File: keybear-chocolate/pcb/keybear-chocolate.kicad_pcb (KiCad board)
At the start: 2 copper layers, 136.9 x 98.2 mm, 108 parts, among them J2 BATT, J3 LED, J4 OLED, P1 USB_C_Plug, SW1 SW_PUSH, SW10 SW_PUSH, SW11 SW_PUSH, SW12 SW_PUSH, SW13 SW_PUSH, SW14 SW_PUSH, SW15 SW_PUSH, SW16 SW_PUSH, SW17 SW_PUSH, SW18 SW_PUSH, SW19 SW_PUSH, SW2 SW_PUSH, SW20 SW_PUSH, SW21 SW_PUSH, SW22 SW_PUSH, SW24 Rotary_Encoder_Switch, SW3 SW_PUSH, SW30 BATT_SW, SW4 SW_PUSH, SW5 SW_PUSH, SW6 SW_PUSH, SW7 SW_PUSH, SW8 SW_PUSH, SW9 SW_PUSH, U1 ProMicro, U2 MCP23017_ML, U3 ATECC608A-SSHDA

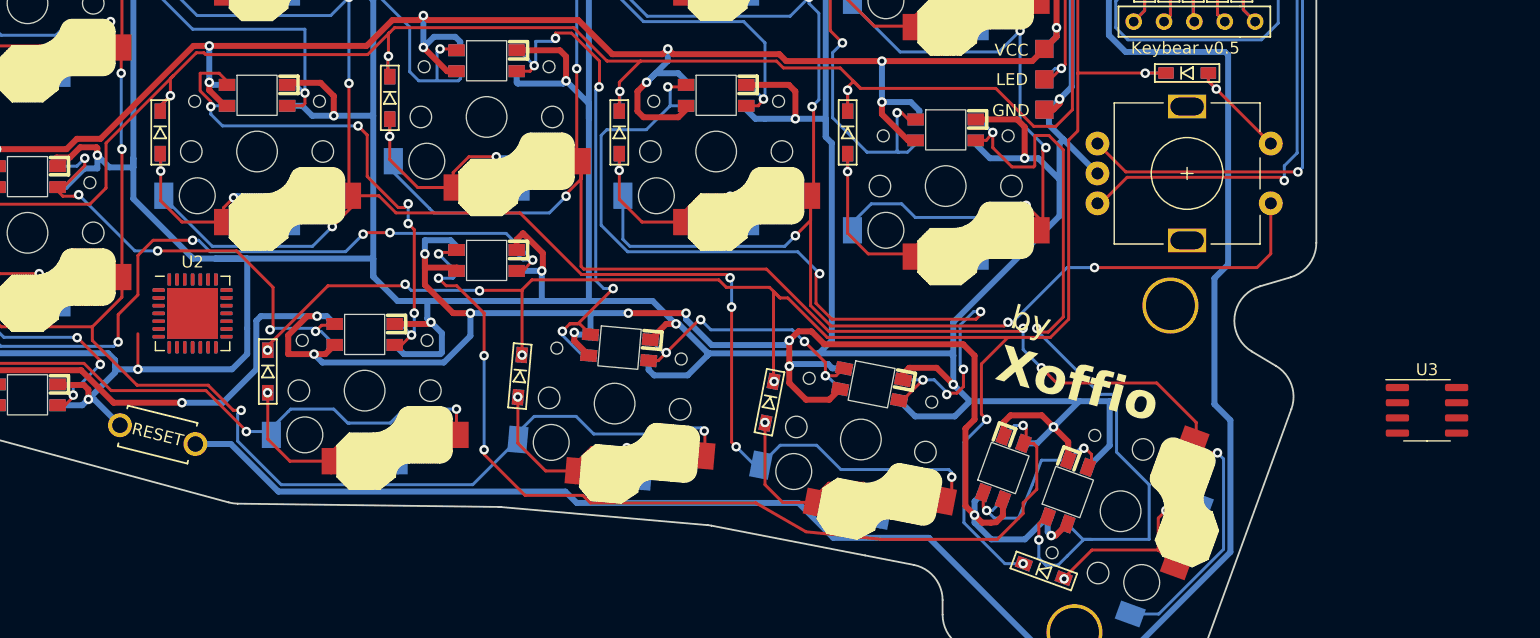
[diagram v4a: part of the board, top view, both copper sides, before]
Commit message: adding PCF8523 (Real Time Clock)
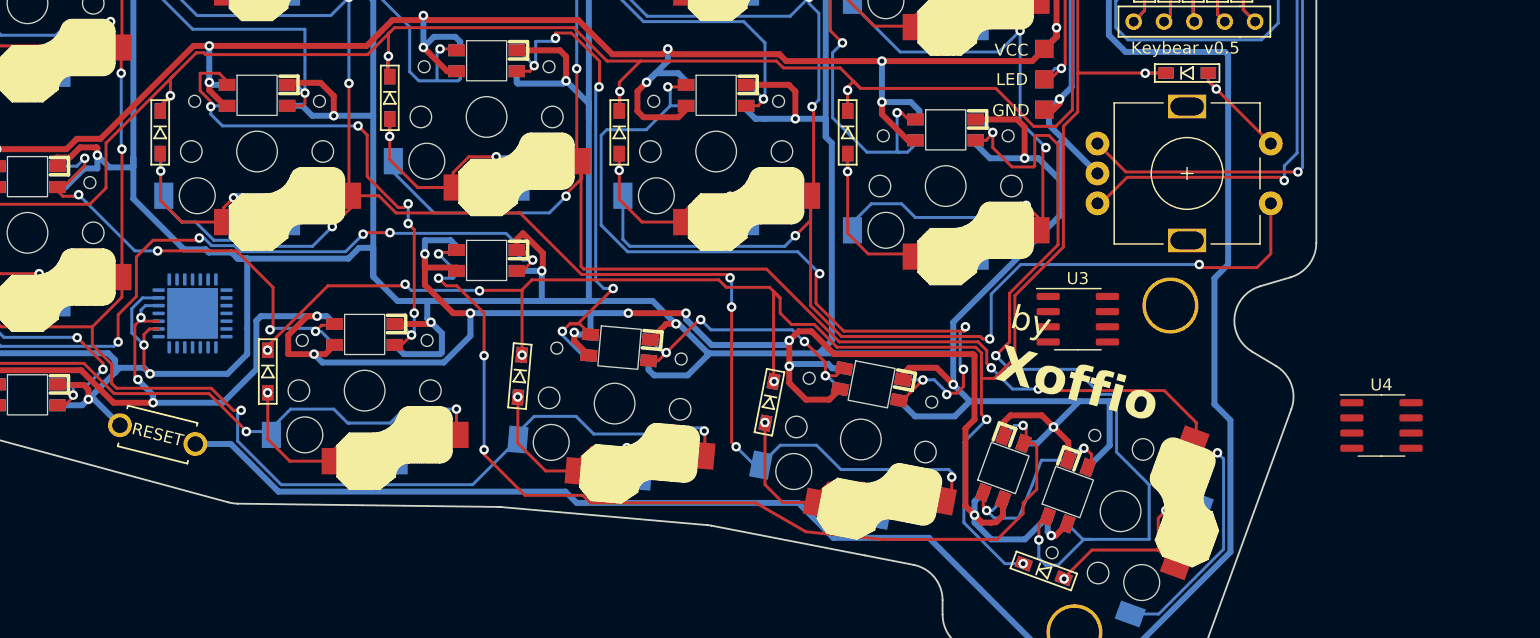
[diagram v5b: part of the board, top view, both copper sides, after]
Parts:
- removed the U2 at (183.0, 156.7)
- added U4: PCF8523T, Package_SO:SOIC-8_3.9x4.9mm_P1.27mm, F.Cu at (282.4, 166.1)
- moved U3 30.2 mm to (257.0, 157.2)
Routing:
- net VCC: track 894.5 -> 906.4 mm, vias 62 -> 64
- net GND: track 914.6 -> 922.4 mm, vias 34 -> 35
- net Net-(L18-DIN): track 71.0 -> 75.7 mm
- net SW24A: track 189.2 -> 192.5 mm
- net Net-(L17-DOUT): track 73.3 -> 70.2 mm
- net col1: track 258.7 -> 259.9 mm
- net row3: track 168.7 -> 169.6 mm
- net col3: track 234.7 -> 234.1 mm
- net Net-(L27-DIN): track 87.3 -> 87.8 mm

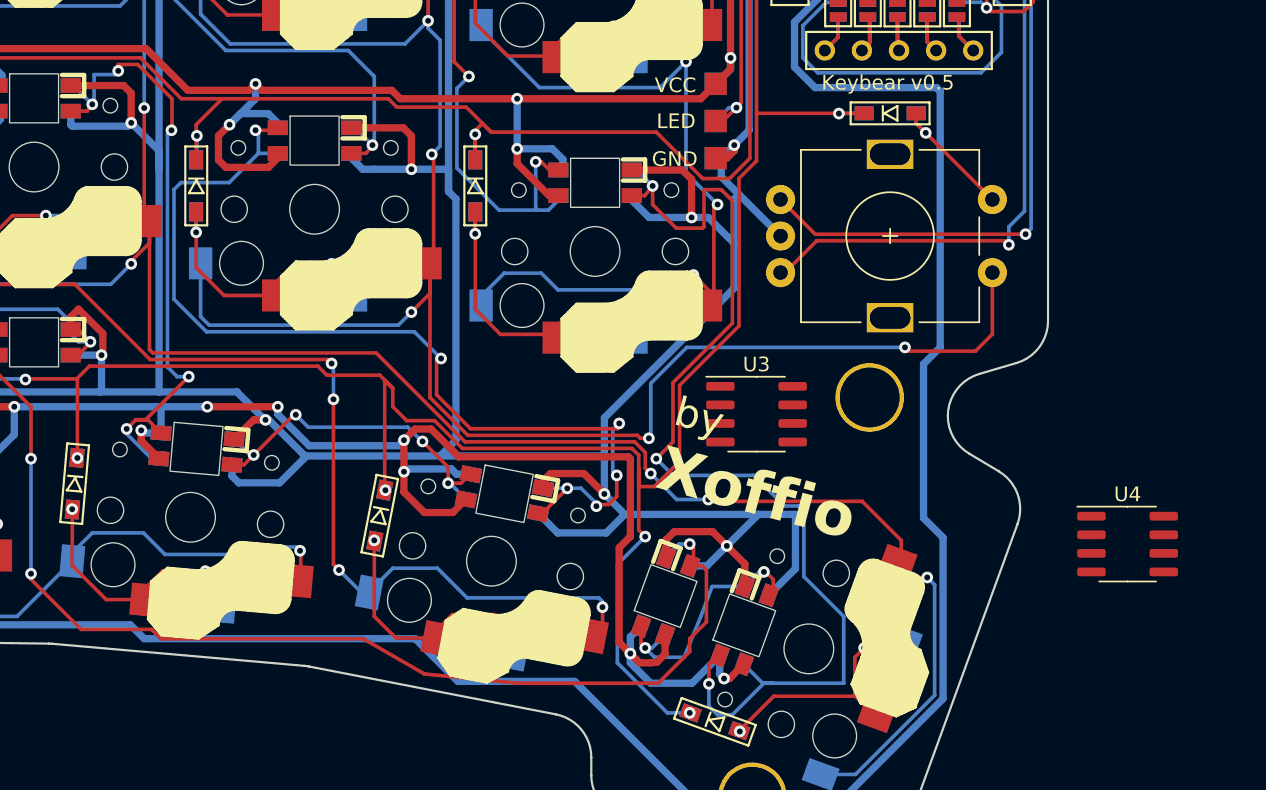
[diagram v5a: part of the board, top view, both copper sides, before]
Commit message: creating connections for the rtc and crypto chip
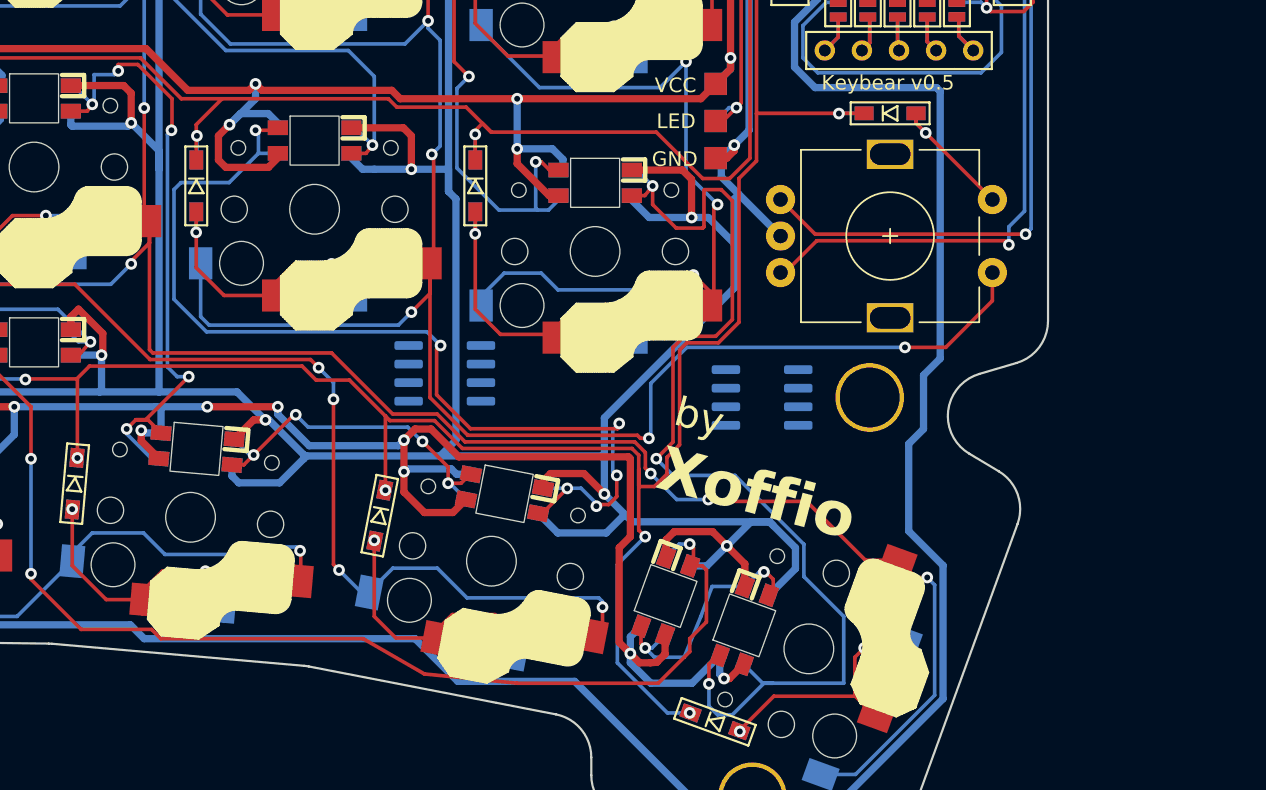
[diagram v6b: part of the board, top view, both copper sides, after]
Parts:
- U3, U4: moved to B.Cu
- moved U4 48.2 mm to (235.7, 154.4), turned to 180 degrees
- moved U3 1.20 mm to (257.4, 156.1), turned to 180 degrees
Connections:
- U3 pad 4: unconnected-(U3-GND-Pad4) -> GND
- U3 pad 5: unconnected-(U3-SDA-Pad5) -> SDA
- U3 pad 6: unconnected-(U3-SCL-Pad6) -> SCL
- U3 pad 8: unconnected-(U3-VCC-Pad8) -> VCC
- U4 pad 4: unconnected-(U4-VSS-Pad4) -> GND
- U4 pad 5: unconnected-(U4-SDA-Pad5) -> SDA
- U4 pad 6: unconnected-(U4-SCL-Pad6) -> SCL
- U4 pad 8: unconnected-(U4-VDD-Pad8) -> VCC
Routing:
- net row3: track 169.6 -> 166.9 mm
- net SW24A: track 192.5 -> 190.9 mm
- net col3: track 234.1 -> 233.1 mm
- net reset: track 184.7 -> 185.6 mm
- net col2: track 238.1 -> 237.4 mm

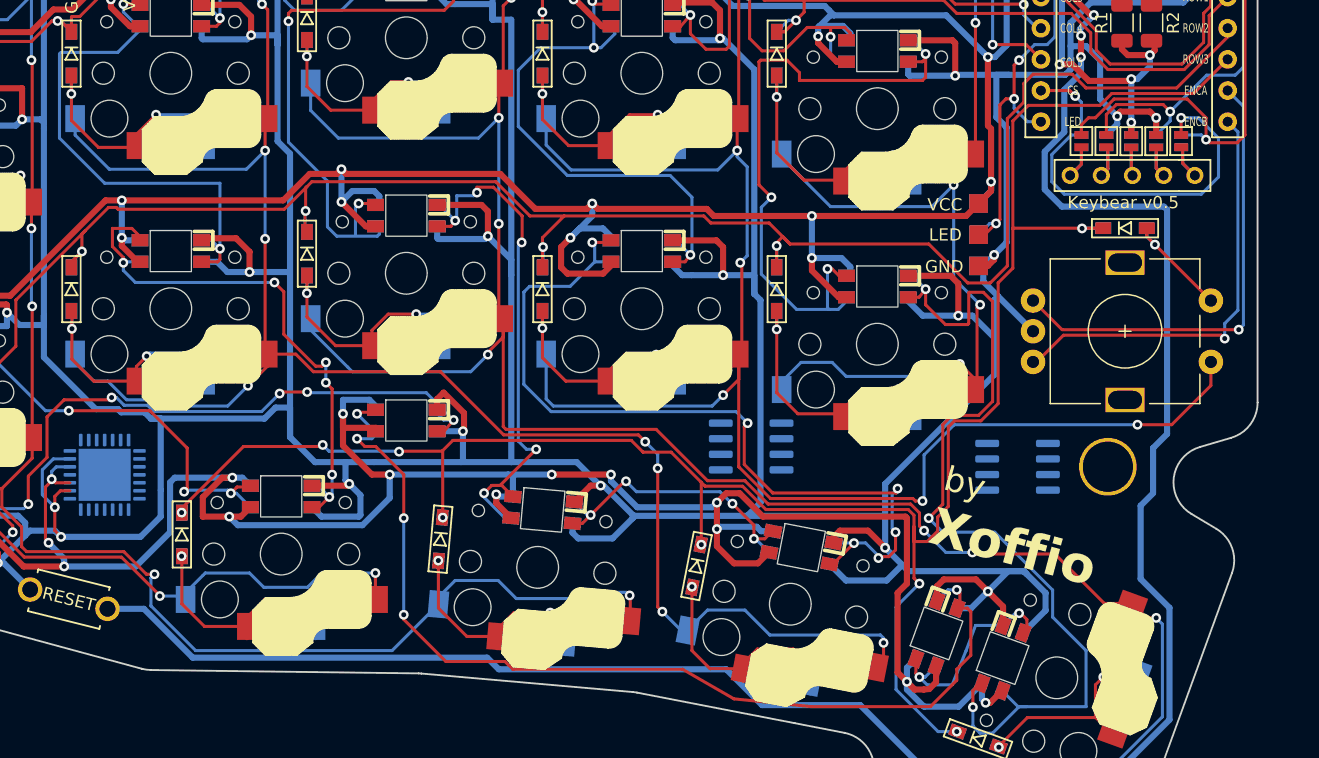
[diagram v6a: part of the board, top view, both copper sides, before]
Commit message: crypto chip connected
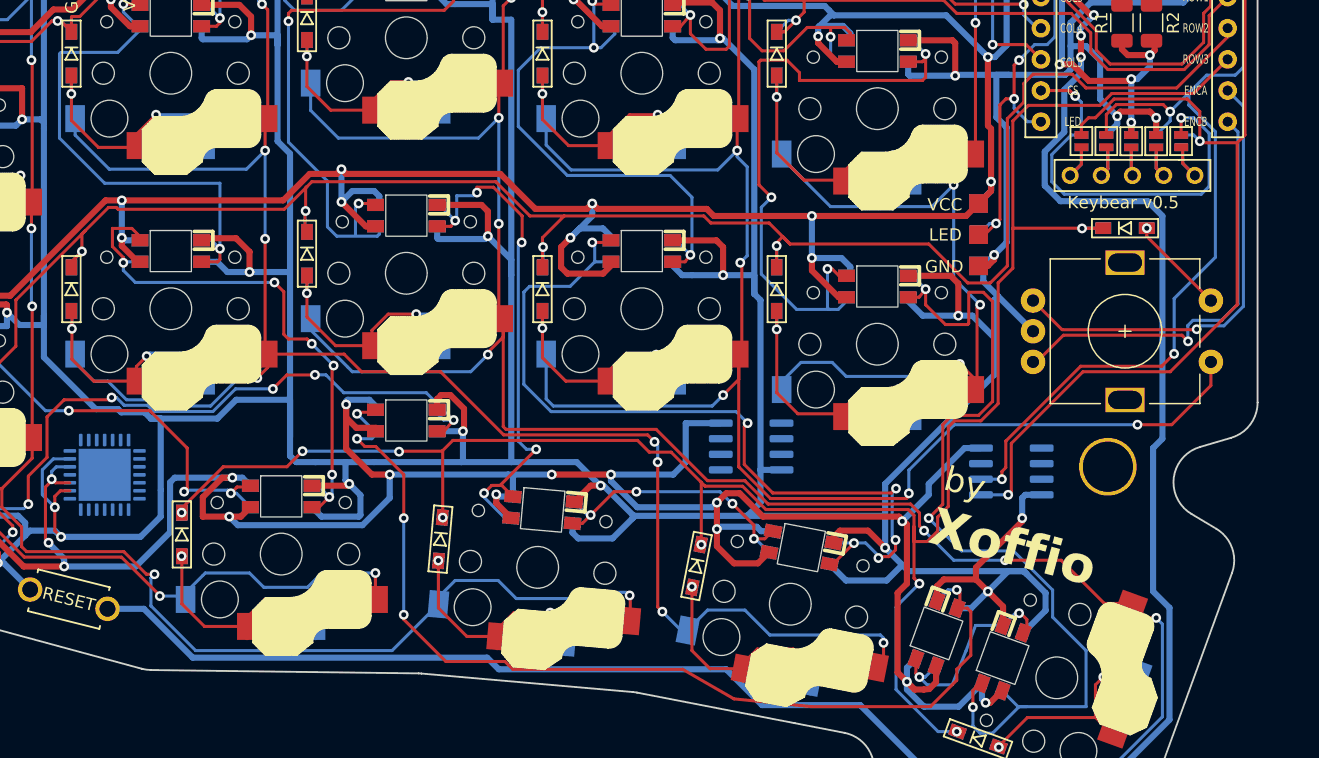
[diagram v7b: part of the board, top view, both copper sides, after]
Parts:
- moved U3 0.63 mm to (256.9, 156.5)
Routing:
- net SCL: track 38.5 -> 83.6 mm, vias 1 -> 3
- net SDA: track 55.4 -> 98.1 mm, vias 3 -> 4
- net VCC: track 906.4 -> 927.6 mm, vias 64 -> 65
- net GND: track 922.0 -> 935.4 mm, vias 35 -> 36
- net reset: track 185.6 -> 183.7 mm
- net SW24B: track 9.68 -> 8.06 mm
- net Net-(L26-DIN): track 70.1 -> 71.2 mm
- net SW24A: track 190.9 -> 189.9 mm
- net ENCA: track 38.9 -> 38.0 mm
- net CS: track 34.5 -> 33.7 mm
- net Net-(L20-DIN): track 24.1 -> 23.4 mm
- net col2: track 237.4 -> 238.0 mm

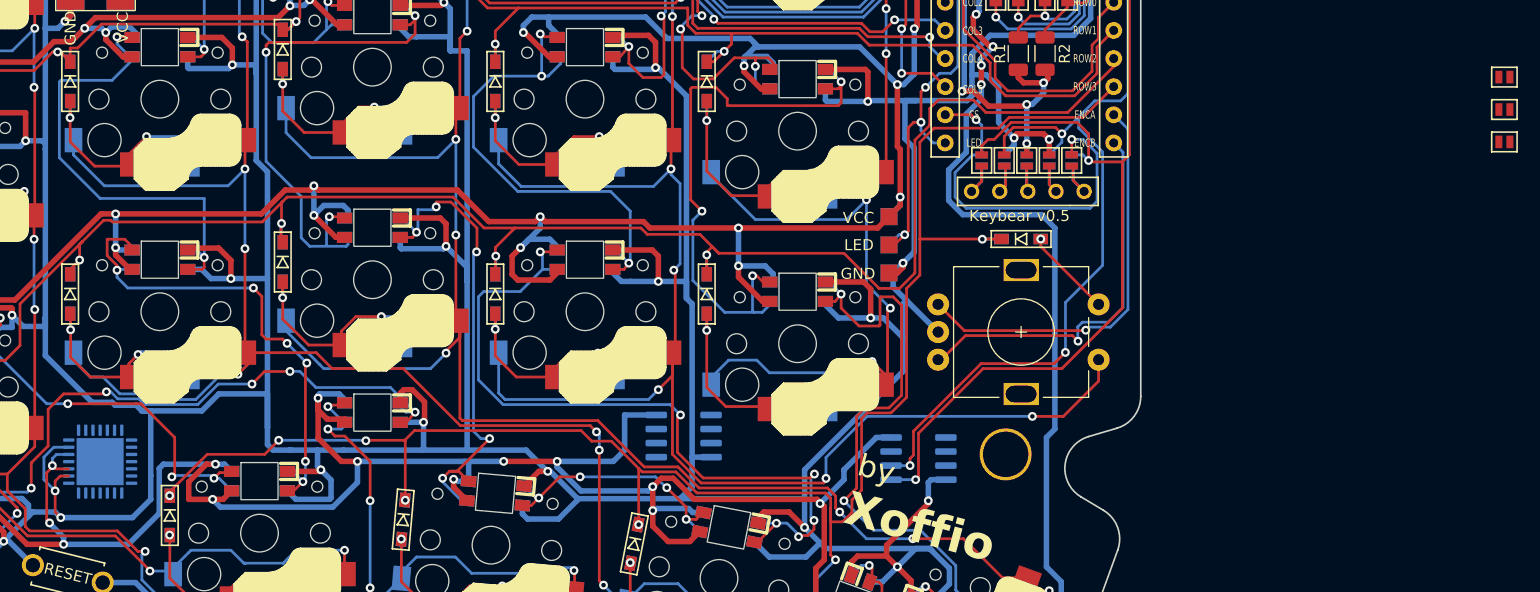
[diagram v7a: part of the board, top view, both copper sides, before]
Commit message: time chip connected. tracks extended
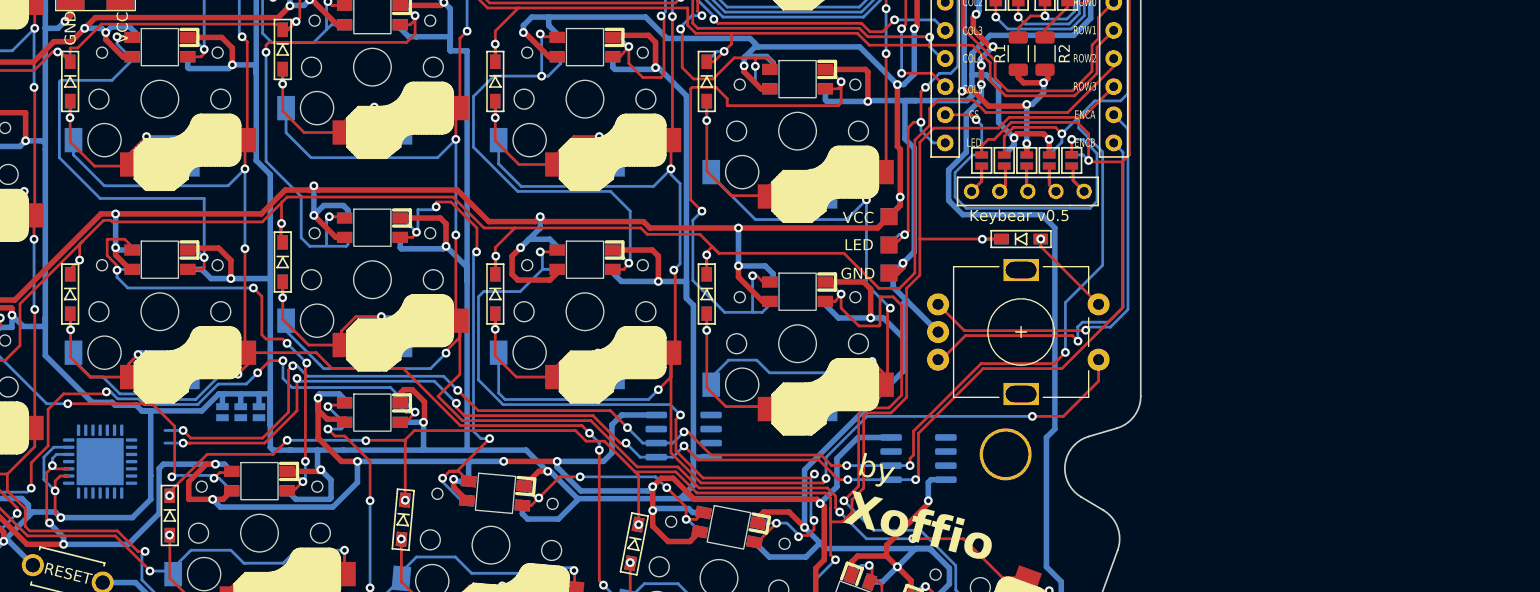
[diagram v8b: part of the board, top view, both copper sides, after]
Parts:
- JP16, JP17, JP18: moved to B.Cu
- moved JP18 118.3 mm to (194.1, 152.3), turned to 90 degrees
- moved JP17 117.4 mm to (195.7, 152.3), turned to 90 degrees
- moved JP16 116.5 mm to (197.4, 152.3), turned to 90 degrees
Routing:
- net SCL: track 83.6 -> 159.0 mm, vias 3 -> 9
- net SDA: track 98.1 -> 173.3 mm, vias 4 -> 10
- net GND: track 935.4 -> 939.2 mm
- net Net-(L26-DIN): track 71.2 -> 73.0 mm
- net col3: track 233.1 -> 234.7 mm
- net VCC: track 927.6 -> 928.2 mm
- net Net-(L14-DIN): track 40.8 -> 41.4 mm
